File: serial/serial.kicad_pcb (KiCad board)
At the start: 2 copper layers, 75.5 x 56.1 mm, 43 parts, among them J1 Conn_02x20_Odd_Even, J2 Conn_01x06_Male, J3 DB9_Male, U1 MC6850, U2 CD4060BE, U3 74LS30, U4 74LS08, U5 74LS02, U6 74LS04, U7 MAX232, Y1 4.0Mhz

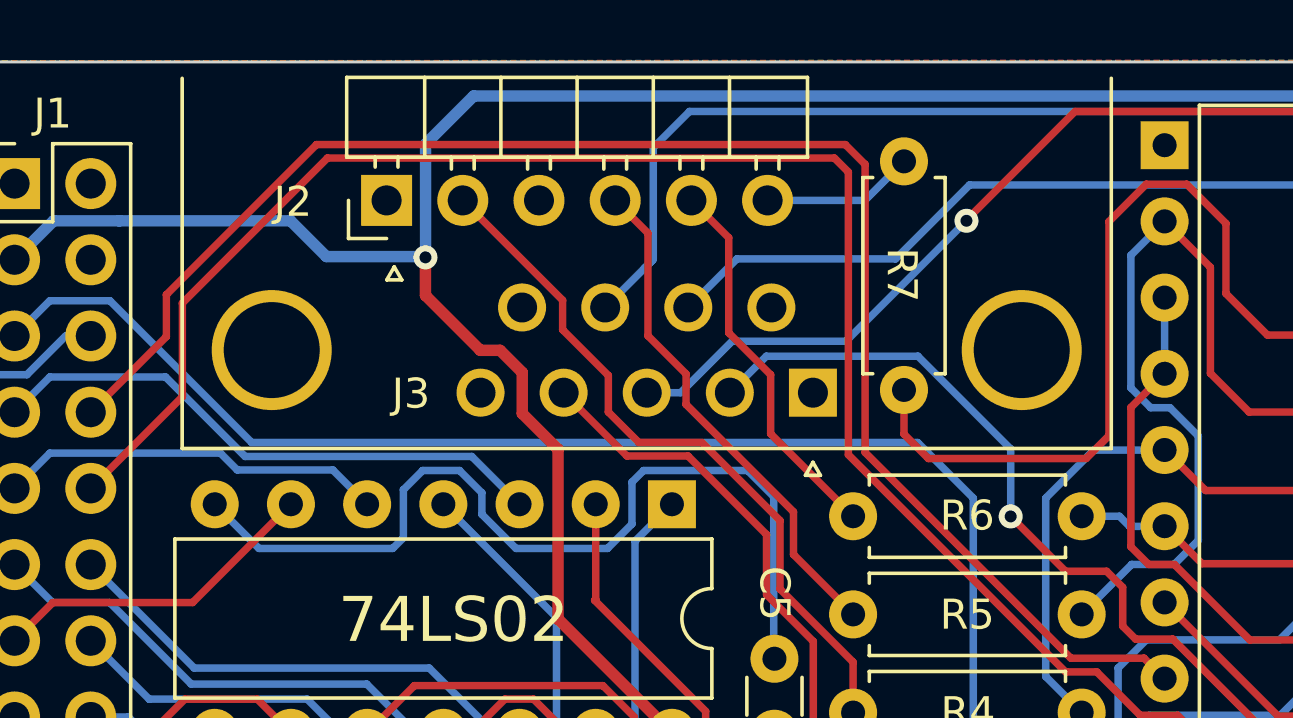
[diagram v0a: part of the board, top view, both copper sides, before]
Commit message: Move DB-9 serial connector fraction closer to PCB edge
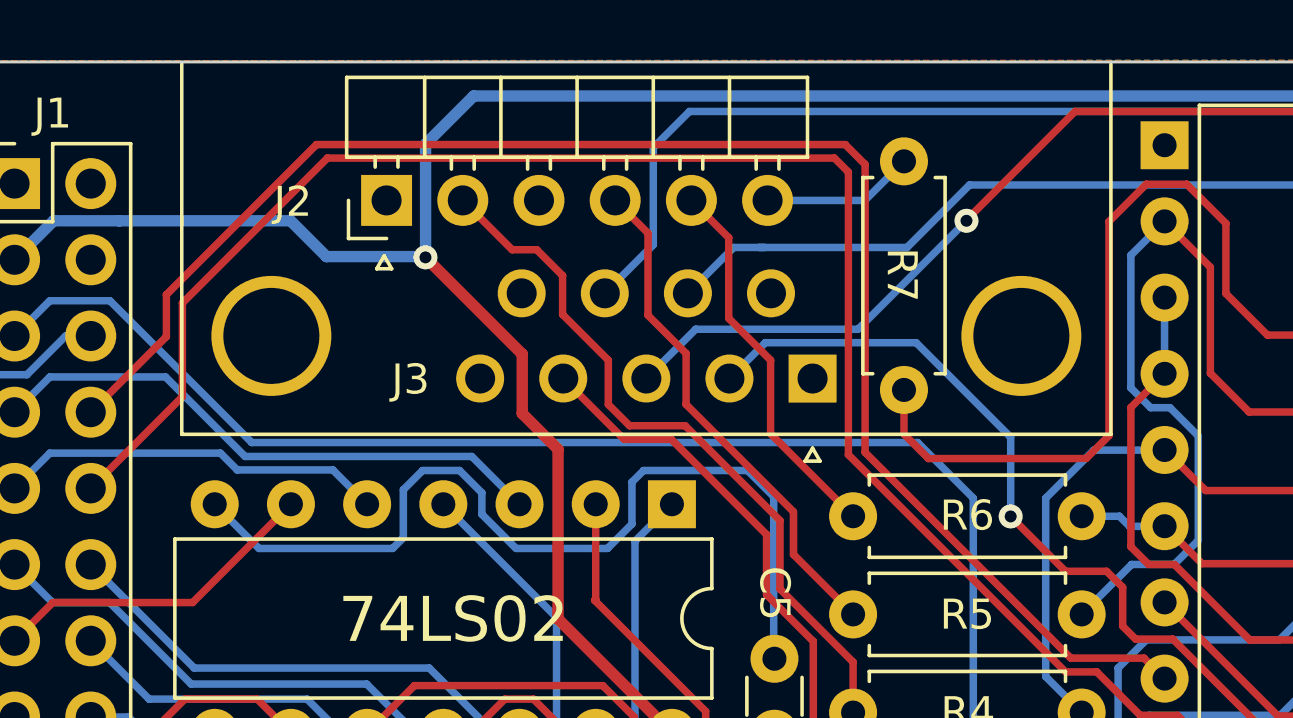
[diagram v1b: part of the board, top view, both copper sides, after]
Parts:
- moved J3 0.47 mm to (129.2, 81.3)
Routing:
- net /CTS: track 71.7 -> 70.8 mm

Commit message: Update design
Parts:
- R3: value 2K7 -> ~
- Y1: footprint Crystal:Crystal_HC49-4H_Vertical -> Crystal:Crystal_HC49-U_Vertical
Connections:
- U1 pad 14: PHI1 -> PHI2
- U2 pad 12: Net-(JP2-Pad10) -> GND
- U6 pad 1: A1 -> GND
- U6 pad 2: Net-(JP1-Pad3) -> unconnected-(U6-Pad2)
- U6 pad 8: unconnected-(U6-Pad8) -> Net-(JP1-Pad3)
- U6 pad 9: GND -> A1
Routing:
- net PHI2: track 0.00 -> 99.2 mm
- net PHI1: track 72.0 -> 0.00 mm
- net Net-(JP2-Pad10): track 52.7 -> 27.5 mm
- net Net-(JP1-Pad3): track 25.2 -> 43.0 mm
- net Net-(JP1-Pad2): track 42.9 -> 27.4 mm
- net A1: track 80.9 -> 93.3 mm
- net R/~{W}: track 83.1 -> 87.2 mm
- net Net-(U1-Pad9): track 66.4 -> 65.0 mm
- net D0: track 74.1 -> 73.2 mm
- net D2: track 70.3 -> 69.4 mm
- net D1: track 68.4 -> 67.5 mm
- net D3: track 64.4 -> 63.8 mm
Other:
- board text added: "Plastic Objects Limited 2022 Rev 1.1A"
- board text removed: "Plastic Objects Limited 2022 Rev 1.0A"
